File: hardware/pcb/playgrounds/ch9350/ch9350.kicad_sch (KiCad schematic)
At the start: 36 parts, among them J1 USB_C_Receptacle_USB2.0_16P, J2 USB_A_Stacked, J3 Conn_02x04_Odd_Even, J4 Conn_02x08_Odd_Even, J5 Conn_02x08_Odd_Even, Q1 MMBT2222A, Q2 MMBT2222A, Q3 MMBT2222A, Q4 MMBT2222A, Q5 MMBT2222A, Q6 MMBT2222A, SW1 SW_Push, SW2 SW_Push, SW3 SW_Push_Dual, U1 CH9350, U2 CH9350

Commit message: ch9350 devboard schematic
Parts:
- R10, R12, R14, R4, R6, R8: footprint (none) -> Resistor_SMD:R_0402_1005Metric; LCSC (none) -> C4260
- R11, R13, R3, R5, R7, R9: LCSC (none) -> C11702

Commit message: ch9350 devboard schematic
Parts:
- R11, R13, R3, R5, R7, R9: footprint (none) -> Resistor_SMD:R_0402_1005Metric

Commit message: ch9350 devboard schematic
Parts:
- J1: value USB_C_Receptacle_USB2.0_16P -> TYPE-C-31-M-12; footprint (none) -> Connector_USB:USB_C_Receptacle_HRO_TYPE-C-31-M-12; LCSC (none) -> C165948
- J2: value USB_A_Stacked -> USB-U267-BWS; footprint (none) -> Connector_USB:USB_A_CUI_UJ2-ADH-TH_Horizontal_Stacked; LCSC (none) -> C2962392
- J3: value Conn_02x04_Odd_Even -> Conn_02x08_Odd_Even; footprint (none) -> Connector_PinHeader_2.54mm:PinHeader_2x08_P2.54mm_Vertical
- J4, J5: value Conn_02x08_Odd_Even -> Conn_02x10_Odd_Even; footprint (none) -> Connector_PinHeader_2.54mm:PinHeader_2x10_P2.54mm_Vertical
- SW1, SW2: value SW_Push -> TS-1187A-B-A-B; footprint (none) -> Button_Switch_SMD:SW_Push_1P1T_XKB_TS-1187A; LCSC (none) -> C318884
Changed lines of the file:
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@@
 			)
 		)
-		(property "Value" "USB_A_Stacked"
+		(property "Value" "USB-U267-BWS"
 			(at 271.78 111.76 0)
 			(effects
@@
 			)
 		)
-		(property "Footprint" ""
+		(property "Footprint" "Connector_USB:USB_A_CUI_UJ2-ADH-TH_Horizontal_Stacked"
 			(at 267.97 140.97 0)
 			(effects
@@
 			)
 		)
+		(property "LCSC" "C2962392"
+			(at 271.78 127 0)
+			(effects
+				(font
+					(size 1.27 1.27)
+				)
+				(hide yes)
+			)
+		)
 		(pin "4"
 		)
@@
 			)
 		)
-		(property "Value" "USB_C_Receptacle_USB2.0_16P"
+		(property "Value" "TYPE-C-31-M-12"
 			(at 210.82 111.76 0)
 			(effects
@@
 			)
 		)
-		(property "Footprint" ""
+		(property "Footprint" "Connector_USB:USB_C_Receptacle_HRO_TYPE-C-31-M-12"
 			(at 214.63 132.08 0)
 			(effects
@@
 			)
 		)
+		(property "LCSC" "C165948"
+			(at 210.82 132.08 0)
+			(effects
+				(font
+					(size 1.27 1.27)
+				)
+				(hide yes)
+			)
+		)
 		(pin "A1"
 		)
@@
 			)
 		)
-		(property "Value" "Conn_02x08_Odd_Even"
+		(property "Value" "Conn_02x10_Odd_Even"
 			(at 138.43 113.03 0)
 			(effects
@@
 			)
 		)
-		(property "Footprint" ""
+		(property "Footprint" "Connector_PinHeader_2.54mm:PinHeader_2x10_P2.54mm_Vertical"
 			(at 137.16 127 0)
 			(effects
@@
 			)
 		)
-		(property "Value" "Conn_02x08_Odd_Even"
+		(property "Value" "Conn_02x10_Odd_Even"
 			(at 62.23 113.03 0)
 			(effects
@@
 			)
 		)
-		(property "Footprint" ""
+		(property "Footprint" "Connector_PinHeader_2.54mm:PinHeader_2x10_P2.54mm_Vertical"
 			(at 60.96 127 0)
 			(effects
@@
 			)
 		)
-		(property "Value" "SW_Push"
+		(property "Value" "TS-1187A-B-A-B"
 			(at 35.56 20.32 0)
 			(effects
@@
 			)
 		)
-		(property "Footprint" ""
+		(property "Footprint" "Button_Switch_SMD:SW_Push_1P1T_XKB_TS-1187A"
 			(at 35.56 20.32 0)
 			(effects
@@
 			)
 		)
+		(property "LCSC" "C318884"
+			(at 35.56 25.4 0)
+			(effects
+				(font
+					(size 1.27 1.27)
+				)
+				(hide yes)
+			)
+		)
 		(pin "2"
 		)
@@
 	)
 	(symbol
-		(lib_id "Switch:SW_Push")
-		(at 35.56 35.56 0)
-		(unit 1)
-		(exclude_from_sim no)
-		(in_bom yes)
-		(on_board yes)
-		(dnp no)
-		(fields_autoplaced yes)
-		(property "Reference" "SW2"
-			(at 35.56 27.94 0)
-			(effects
-				(font
-					(size 1.27 1.27)
-				)
-			)
-		)
-		(property "Value" "SW_Push"
-			(at 35.56 30.48 0)
-			(effects
-				(font
-					(size 1.27 1.27)
-				)
-			)
-		)
-		(property "Footprint" ""
-			(at 35.56 30.48 0)
-			(effects
-				(font
-					(size 1.27 1.27)
-				)
-				(hide yes)
-			)
-		)
-		(property "Datasheet" "~"
-			(at 35.56 30.48 0)
-			(effects
-				(font
-					(size 1.27 1.27)
-				)
-				(hide yes)
-			)
-		)
-		(property "Description" "Push button switch, generic, two pins"
-			(at 35.56 35.56 0)
-			(effects
-				(font
-					(size 1.27 1.27)
-				)
-				(hide yes)
-			)
-		)
-		(pin "2"
-		)
-		(pin "1"
-		)
-		(instances
-			(project "ch9350"
-				(path "/7f205840-aa3b-4791-816b-13824847f659"
-					(reference "SW2")
-					(unit 1)
-				)
-			)
-		)
-	)
-	(symbol
 		(lib_id "Device:LED_Small")
 		(at 60.96 165.1 90)
@@
 			)
 		)
-		(property "Value" "Conn_02x04_Odd_Even"
+		(property "Value" "Conn_02x08_Odd_Even"
 			(at 100.33 113.03 0)
 			(effects
@@
 			)
 		)
-		(property "Footprint" ""
+		(property "Footprint" "Connector_PinHeader_2.54mm:PinHeader_2x08_P2.54mm_Vertical"
 			(at 99.06 124.46 0)
 			(effects
@@
 					(unit 1)
 				)
+			)
+		)
+	)
+	(symbol
+		(lib_id "Switch:SW_Push")
+		(at 35.56 35.56 0)
+		(unit 1)
+		(exclude_from_sim no)
+		(in_bom yes)
+		(on_board yes)
+		(dnp no)
+		(fields_autoplaced yes)
+		(property "Reference" "SW2"
+			(at 35.56 27.94 0)
+			(effects
+				(font
+					(size 1.27 1.27)
+				)
+			)
+		)
+		(property "Value" "TS-1187A-B-A-B"
+			(at 35.56 30.48 0)
+			(effects
+				(font
+					(size 1.27 1.27)
+				)
+			)
+		)
+		(property "Footprint" "Button_Switch_SMD:SW_Push_1P1T_XKB_TS-1187A"
+			(at 35.56 30.48 0)
+			(effects
+				(font
+					(size 1.27 1.27)
+				)
+				(hide yes)
+			)
+		)
+		(property "Datasheet" "~"
+			(at 35.56 30.48 0)
+			(effects
+				(font
+					(size 1.27 1.27)
+				)
+				(hide yes)
+			)
+		)
+		(property "Description" "Push button switch, generic, two pins"
+			(at 35.56 35.56 0)
+			(effects
+				(font
+					(size 1.27 1.27)
+				)
+				(hide yes)
+			)
+		)
+		(property "LCSC" "C318884"
+			(at 35.56 35.56 0)
+			(effects
+				(font
+					(size 1.27 1.27)
+				)
+				(hide yes)
+			)
+		)
+		(pin "2"
+		)
+		(pin "1"
+		)
+		(instances
+			(project "ch9350"
+				(path "/7f205840-aa3b-4791-816b-13824847f659"
+					(reference "SW2")
+					(unit 1)
+				)

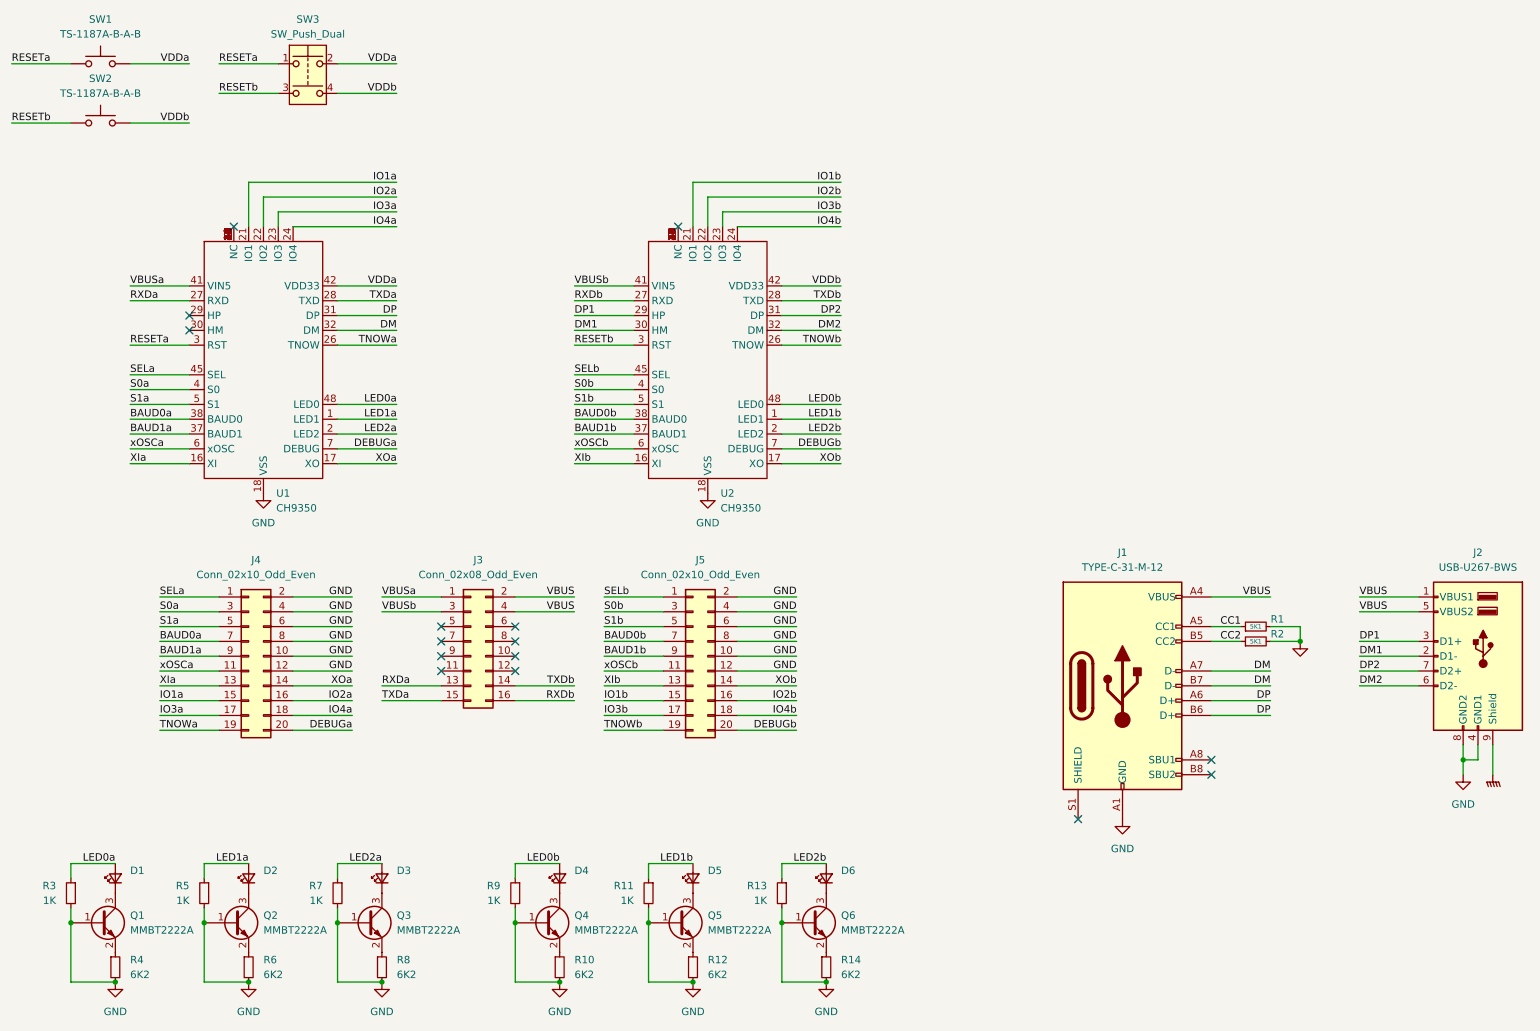
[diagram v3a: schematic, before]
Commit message: ch9350 devboard layout
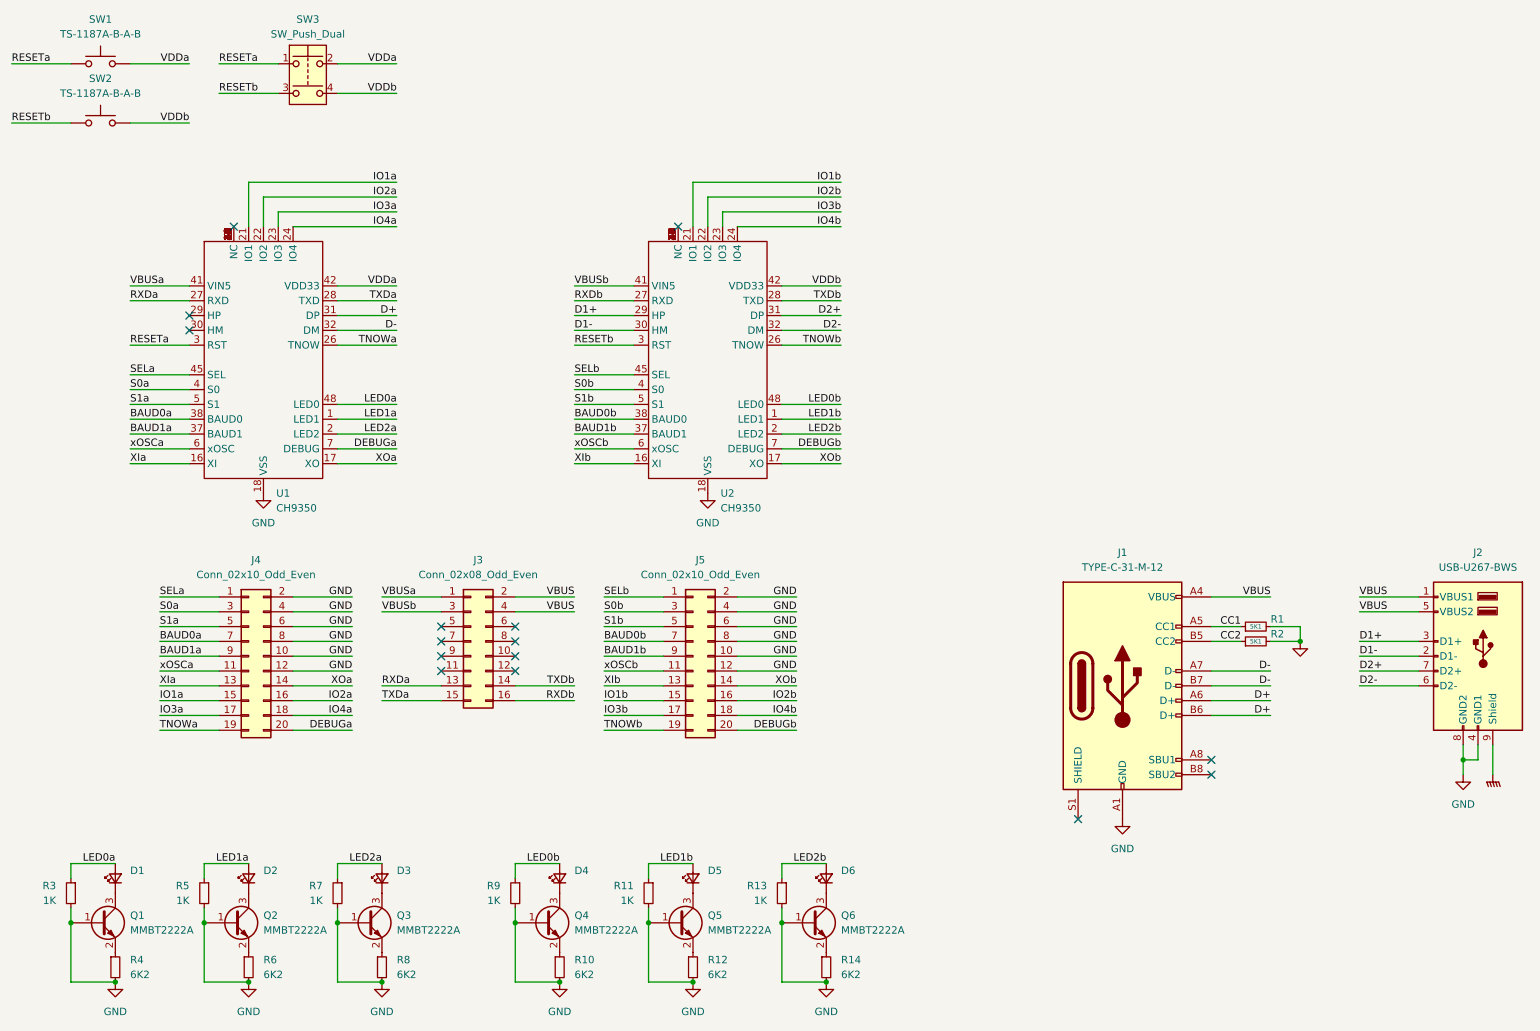
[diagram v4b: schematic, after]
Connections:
- net DM renamed D-
- net DM1 renamed D1-
- net DM2 renamed D2-
- net DP renamed D+
- net DP1 renamed D1+
- net DP2 renamed D2+
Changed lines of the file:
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@@
 		)
 	)
-	(label "DP"
+	(label "D+"
 		(at 236.22 137.16 180)
 		(fields_autoplaced yes)
@@
 		)
 	)
-	(label "DP2"
+	(label "D2+"
 		(at 251.46 129.54 0)
 		(fields_autoplaced yes)
@@
 		)
 	)
-	(label "DM2"
+	(label "D2-"
 		(at 162.56 71.12 180)
 		(fields_autoplaced yes)
@@
 		)
 	)
-	(label "DP1"
+	(label "D1+"
 		(at 251.46 124.46 0)
 		(fields_autoplaced yes)
@@
 		)
 	)
-	(label "DP"
+	(label "D+"
 		(at 236.22 134.62 180)
 		(fields_autoplaced yes)
@@
 		)
 	)
-	(label "DM1"
+	(label "D1-"
 		(at 116.84 71.12 0)
 		(fields_autoplaced yes)
@@
 		)
 	)
-	(label "DP2"
+	(label "D2+"
 		(at 162.56 68.58 180)
 		(fields_autoplaced yes)
@@
 		)
 	)
-	(label "DP1"
+	(label "D1+"
 		(at 116.84 68.58 0)
 		(fields_autoplaced yes)
@@
 		)
 	)
-	(label "DM"
+	(label "D-"
 		(at 236.22 132.08 180)
 		(fields_autoplaced yes)
@@
 		)
 	)
-	(label "DM2"
+	(label "D2-"
 		(at 251.46 132.08 0)
 		(fields_autoplaced yes)
@@
 		)
 	)
-	(label "DM1"
+	(label "D1-"
 		(at 251.46 127 0)
 		(fields_autoplaced yes)
@@
 		)
 	)
-	(label "DM"
+	(label "D-"
 		(at 86.36 71.12 180)
 		(fields_autoplaced yes)
@@
 		)
 	)
-	(label "DP"
+	(label "D+"
 		(at 86.36 68.58 180)
 		(fields_autoplaced yes)
@@
 		)
 	)
-	(label "DM"
+	(label "D-"
 		(at 236.22 129.54 180)
 		(fields_autoplaced yes)

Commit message: ch9350 devboard layout 2
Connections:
- net RXDa: now also J3.16 (Pin_16); no longer J3.13 (Pin_13)
- net RXDb: now also J3.13 (Pin_13); no longer J3.16 (Pin_16)
- net TXDa: now also J3.14 (Pin_14); no longer J3.15 (Pin_15)
- net TXDb: now also J3.15 (Pin_15); no longer J3.14 (Pin_14)
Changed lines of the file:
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@@
 		)
 	)
-	(label "RXDa"
+	(label "RXDb"
 		(at 83.82 132.08 0)
 		(fields_autoplaced yes)
@@
 		)
 	)
-	(label "TXDb"
+	(label "TXDa"
 		(at 116.84 132.08 180)
 		(fields_autoplaced yes)
@@
 		)
 	)
-	(label "RXDb"
+	(label "RXDa"
 		(at 116.84 134.62 180)
 		(fields_autoplaced yes)
@@
 		)
 	)
-	(label "TXDa"
+	(label "TXDb"
 		(at 83.82 134.62 0)
 		(fields_autoplaced yes)

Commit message: ch9350 devboard layout 3?
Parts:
- removed J3: Conn_02x08_Odd_Even, Connector_PinHeader_2.54mm:PinHeader_2x08_P2.54mm_Vertical, symbol Connector_Generic:Conn_02x08_Odd_Even
- removed J4, J5: Conn_02x10_Odd_Even, Connector_PinHeader_2.54mm:PinHeader_2x10_P2.54mm_Vertical, symbol Connector_Generic:Conn_02x10_Odd_Even
- removed SW3: SW_Push_Dual, symbol Switch:SW_Push_Dual
- added C1, C3: 4u7F, Capacitor_SMD:C_0402_1005Metric, symbol Device:C_Small
- added C2, C4: 100nF, Capacitor_SMD:C_0402_1005Metric, symbol Device:C_Small
- added J10, J6: Conn_01x04, Connector_PinHeader_2.54mm:PinHeader_1x04_P2.54mm_Vertical, symbol Connector_Generic:Conn_01x04
- added J3, J7: Conn_01x06, Connector_PinHeader_2.54mm:PinHeader_1x06_P2.54mm_Vertical, symbol Connector_Generic:Conn_01x06
- added J4, J8: Conn_02x08, Connector_PinHeader_2.54mm:PinHeader_2x08_P2.54mm_Vertical, symbol Connector_Generic:Conn_02x08_Odd_Even
- added J5, J9: Conn_02x05, Connector_PinHeader_2.54mm:PinHeader_2x05_P2.54mm_Vertical, symbol Connector_Generic:Conn_02x05_Odd_Even
- U1, U2: value CH9350 -> CH9350L; LCSC (none) -> C109472
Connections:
- net BAUD0a: now also J5.4 (Pin_4)
- net BAUD0b: now also J9.4 (Pin_4)
- net BAUD1a: now also J5.2 (Pin_2)
- net BAUD1b: now also J9.2 (Pin_2)
- net D1+: now also U2.31 (DP); no longer U2.29 (HP)
- net D1-: now also U2.32 (DM); no longer U2.30 (HM)
- net D2+: now also U2.29 (HP); no longer U2.31 (DP)
- net D2-: now also U2.30 (HM); no longer U2.32 (DM)
- net DEBUGa: now also J4.16 (Pin_16)
- net DEBUGb: now also J8.16 (Pin_16)
- net GND: now also C1.2, C2.1, C3.2, C4.1, J10.4 (Pin_4), J4.11 (Pin_11), J4.13 (Pin_13), J4.9 (Pin_9), J5.1 (Pin_1), J5.3 (Pin_3), J5.9 (Pin_9), J6.4 (Pin_4), J8.11 (Pin_11), J8.13 (Pin_13), J8.9 (Pin_9), J9.1 (Pin_1), J9.3 (Pin_3), J9.9 (Pin_9)
- net IO1a: now also J3.3 (Pin_3)
- net IO1b: now also J7.3 (Pin_3)
- net IO2a: now also J3.4 (Pin_4)
- net IO2b: now also J7.4 (Pin_4)
- net IO3a: now also J3.5 (Pin_5)
- net IO3b: now also J7.5 (Pin_5)
- net IO4a: now also J3.6 (Pin_6)
- net IO4b: now also J7.6 (Pin_6)
- net LED0a: now also J4.2 (Pin_2); no longer D1.2 (A), R3.1
- net LED0b: now also J8.2 (Pin_2); no longer D4.2 (A), R9.1
- net LED1a: now also J4.4 (Pin_4); no longer D2.2 (A), R5.1
- net LED1b: now also J8.4 (Pin_4); no longer D5.2 (A), R11.1
- net LED2a: now also J4.6 (Pin_6); no longer D3.2 (A), R7.1
- net LED2b: now also J8.6 (Pin_6); no longer D6.2 (A), R13.1
- net RESETa: now also J4.8 (Pin_8)
- net RESETb: now also J8.8 (Pin_8)
- net RXDa: now also J6.2 (Pin_2)
- net RXDb: now also J10.2 (Pin_2)
- net S0a: now also J4.10 (Pin_10)
- net S0b: now also J8.10 (Pin_10)
- net S1a: now also J4.12 (Pin_12)
- net S1b: now also J8.12 (Pin_12)
- net SELa: now also J5.10 (Pin_10)
- net SELb: now also J9.10 (Pin_10)
- net TNOWa: now also J6.1 (Pin_1)
- net TNOWb: now also J10.1 (Pin_1)
- net TXDa: now also J6.3 (Pin_3)
- net TXDb: now also J10.3 (Pin_3)
- net VBUS: now also J5.5 (Pin_5), J9.5 (Pin_5)
- net VBUSa: now also C2.2, J5.6 (Pin_6)
- net VBUSb: now also C4.2, J9.6 (Pin_6)
- net VDDa: now also C1.1, J4.7 (Pin_7), J5.8 (Pin_8)
- net VDDb: now also C3.1, J8.7 (Pin_7), J9.8 (Pin_8)
- net XIa: now also J3.1 (Pin_1)
- net XIb: now also J7.1 (Pin_1)
- net XOa: now also J3.2 (Pin_2)
- net XOb: now also J7.2 (Pin_2)
- net xOSCa: now also J4.14 (Pin_14)
- net xOSCb: now also J8.14 (Pin_14)
- new net JLED0a: D1.2 (A), J4.1 (Pin_1), R3.1
- new net JLED0b: D4.2 (A), J8.1 (Pin_1), R9.1
- new net JLED1a: D2.2 (A), J4.3 (Pin_3), R5.1
- new net JLED1b: D5.2 (A), J8.3 (Pin_3), R11.1
- new net JLED2a: D3.2 (A), J4.5 (Pin_5), R7.1
- new net JLED2b: D6.2 (A), J8.5 (Pin_5), R13.1
- new net JVDDa: J5.7 (Pin_7)
- new net JVDDb: J9.7 (Pin_7)
- no-connect marks 15 -> 9
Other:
- moved on the sheet: U2
